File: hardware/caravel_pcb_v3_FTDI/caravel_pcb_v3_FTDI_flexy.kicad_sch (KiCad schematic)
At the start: 60 parts, among them J1 USB_B_Micro - 10118193-0001LF, J10 Conn_01x27_Female, J11 Conn_01x20_Female, J2 Conn_01x02_Female, J3 Conn_01x02_Female, J5 Conn_01x02_Male, J6 Conn_01x02_Male, J7 Conn_01x06_Female, J8 Conn_01x02_Male, J9 Conn_01x02_Male, SW1 SW_Push - SKQGADE010, T1 Logo, T2 Logo, U1 FT232H, U2 SN74LVC1G125DCKR, U3 SN74LVC1G125DCKR, U4 AZ1117CH-1.8TRG1, U5 AZ1117-3.3, U6 caravel_breakout, U7 W25Q32FVSS, X1 DSC6001_10MHZ, Y1 CSTNE12M0GH5L000R0

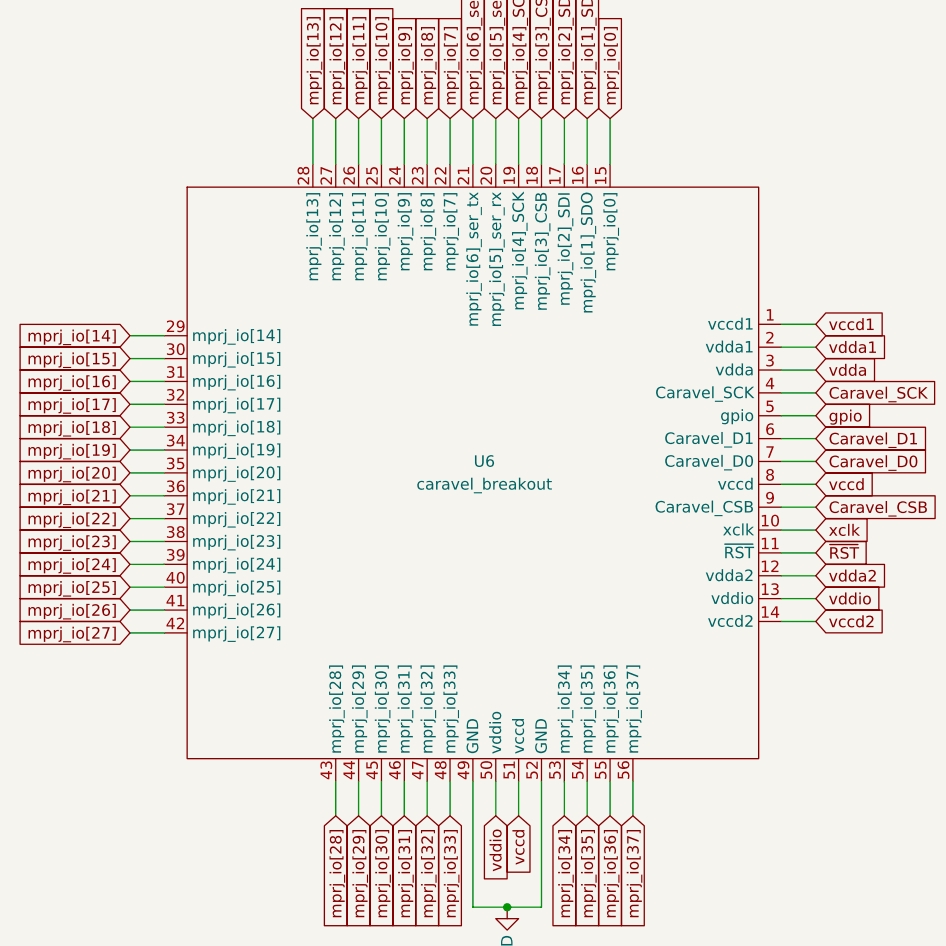
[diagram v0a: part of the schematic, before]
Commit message: fix caravel breakout pin mismatch
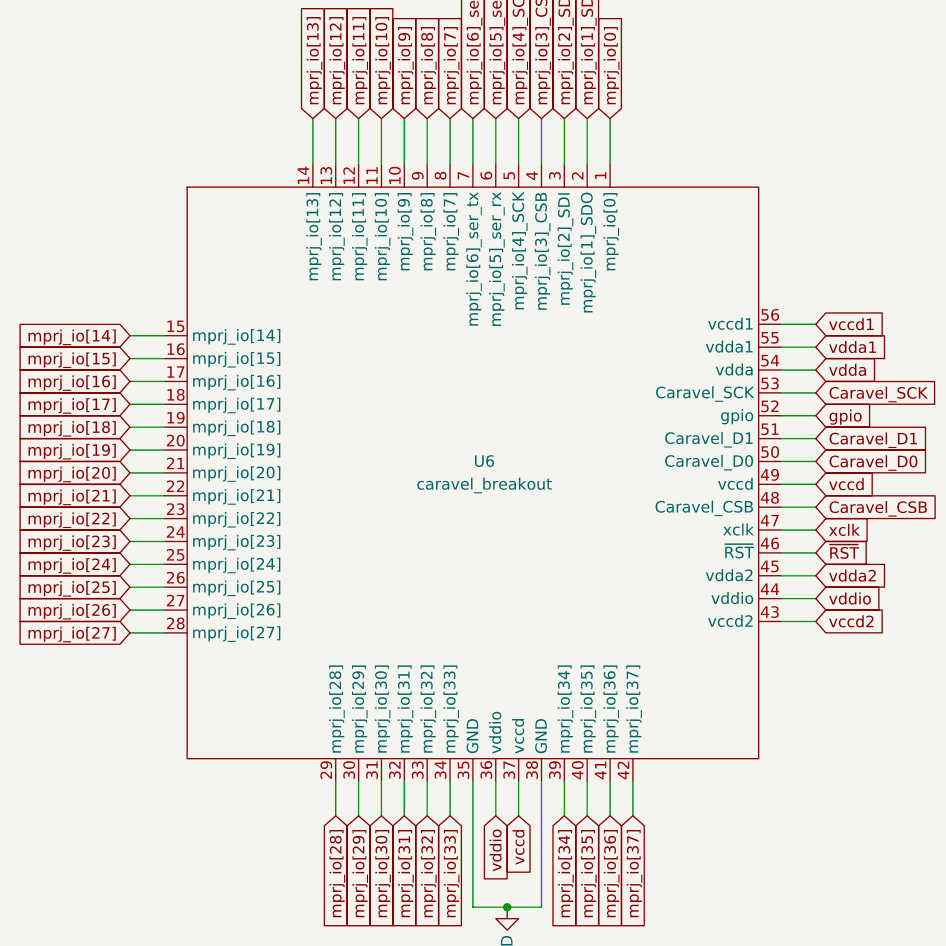
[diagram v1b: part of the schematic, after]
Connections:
- net +1V8: now also U6.37 (vccd), U6.49 (vccd); no longer U6.51 (vccd), U6.8 (vccd)
- net +3V3: now also U6.36 (vddio), U6.44 (vddio), U6.54 (vdda); no longer U6.13 (vddio), U6.3 (vdda), U6.50 (vddio)
- net Caravel_CSB: now also U6.48 (Caravel_CSB); no longer U6.9 (Caravel_CSB)
- net Caravel_D0: now also U6.50 (Caravel_D0); no longer U6.7 (Caravel_D0)
- net Caravel_D1: now also U6.51 (Caravel_D1); no longer U6.6 (Caravel_D1)
- net Caravel_SCK: now also U6.53 (Caravel_SCK); no longer U6.4 (Caravel_SCK)
- net GND: now also U6.35 (GND), U6.38 (GND); no longer U6.49 (GND), U6.52 (GND)
- net USB_CS1: now also U6.4 (mprj_io[3]_CSB); no longer U6.18 (mprj_io[3]_CSB)
- net USB_SCK_TXD: now also U6.5 (mprj_io[4]_SCK); no longer U6.19 (mprj_io[4]_SCK)
- net USB_SI: now also U6.2 (mprj_io[1]_SDO); no longer U6.16 (mprj_io[1]_SDO)
- net USB_SO_RXD: now also U6.3 (mprj_io[2]_SDI); no longer U6.17 (mprj_io[2]_SDI)
- net gpio: now also U6.52 (gpio); no longer U6.5 (gpio)
- net mprj_io[0]: now also U6.1 (mprj_io[0]); no longer U6.15 (mprj_io[0])
- net mprj_io[10]: now also U6.11 (mprj_io[10]); no longer U6.25 (mprj_io[10])
- net mprj_io[11]: now also U6.12 (mprj_io[11]); no longer U6.26 (mprj_io[11])
- net mprj_io[12]: now also U6.13 (mprj_io[12]); no longer U6.27 (mprj_io[12])
- net mprj_io[13]: now also U6.14 (mprj_io[13]); no longer U6.28 (mprj_io[13])
- net mprj_io[14]: now also U6.15 (mprj_io[14]); no longer U6.29 (mprj_io[14])
- net mprj_io[15]: now also U6.16 (mprj_io[15]); no longer U6.30 (mprj_io[15])
- net mprj_io[16]: now also U6.17 (mprj_io[16]); no longer U6.31 (mprj_io[16])
- net mprj_io[17]: now also U6.18 (mprj_io[17]); no longer U6.32 (mprj_io[17])
- net mprj_io[18]: now also U6.19 (mprj_io[18]); no longer U6.33 (mprj_io[18])
- net mprj_io[19]: now also U6.20 (mprj_io[19]); no longer U6.34 (mprj_io[19])
- net mprj_io[20]: now also U6.21 (mprj_io[20]); no longer U6.35 (mprj_io[20])
- net mprj_io[21]: now also U6.22 (mprj_io[21]); no longer U6.36 (mprj_io[21])
- net mprj_io[22]: now also U6.23 (mprj_io[22]); no longer U6.37 (mprj_io[22])
- net mprj_io[23]: now also U6.24 (mprj_io[23]); no longer U6.38 (mprj_io[23])
- net mprj_io[24]: now also U6.25 (mprj_io[24]); no longer U6.39 (mprj_io[24])
- net mprj_io[25]: now also U6.26 (mprj_io[25]); no longer U6.40 (mprj_io[25])
- net mprj_io[26]: now also U6.27 (mprj_io[26]); no longer U6.41 (mprj_io[26])
- net mprj_io[27]: now also U6.28 (mprj_io[27]); no longer U6.42 (mprj_io[27])
- net mprj_io[28]: now also U6.29 (mprj_io[28]); no longer U6.43 (mprj_io[28])
- net mprj_io[29]: now also U6.30 (mprj_io[29]); no longer U6.44 (mprj_io[29])
- net mprj_io[30]: now also U6.31 (mprj_io[30]); no longer U6.45 (mprj_io[30])
- net mprj_io[31]: now also U6.32 (mprj_io[31]); no longer U6.46 (mprj_io[31])
- net mprj_io[32]: now also U6.33 (mprj_io[32]); no longer U6.47 (mprj_io[32])
- net mprj_io[33]: now also U6.34 (mprj_io[33]); no longer U6.48 (mprj_io[33])
- net mprj_io[34]: now also U6.39 (mprj_io[34]); no longer U6.53 (mprj_io[34])
- net mprj_io[35]: now also U6.40 (mprj_io[35]); no longer U6.54 (mprj_io[35])
- net mprj_io[36]: now also U6.41 (mprj_io[36]); no longer U6.55 (mprj_io[36])
- net mprj_io[37]: now also U6.42 (mprj_io[37]); no longer U6.56 (mprj_io[37])
- net mprj_io[5]_ser_rx: now also U6.6 (mprj_io[5]_ser_rx); no longer U6.20 (mprj_io[5]_ser_rx)
- net mprj_io[6]_ser_tx: now also U6.7 (mprj_io[6]_ser_tx); no longer U6.21 (mprj_io[6]_ser_tx)
- net mprj_io[7]: now also U6.8 (mprj_io[7]); no longer U6.22 (mprj_io[7])
- net mprj_io[8]: now also U6.9 (mprj_io[8]); no longer U6.23 (mprj_io[8])
- net mprj_io[9]: now also U6.10 (mprj_io[9]); no longer U6.24 (mprj_io[9])
- net vccd1: now also U6.56 (vccd1); no longer U6.1 (vccd1)
- net vccd2: now also U6.43 (vccd2); no longer U6.14 (vccd2)
- net vdda1: now also U6.55 (vdda1); no longer U6.2 (vdda1)
- net vdda2: now also U6.45 (vdda2); no longer U6.12 (vdda2)
- net xclk: now also U6.47 (xclk); no longer U6.10 (xclk)
- net ~{RST}: now also U6.46 (~{RST}); no longer U6.11 (~{RST})

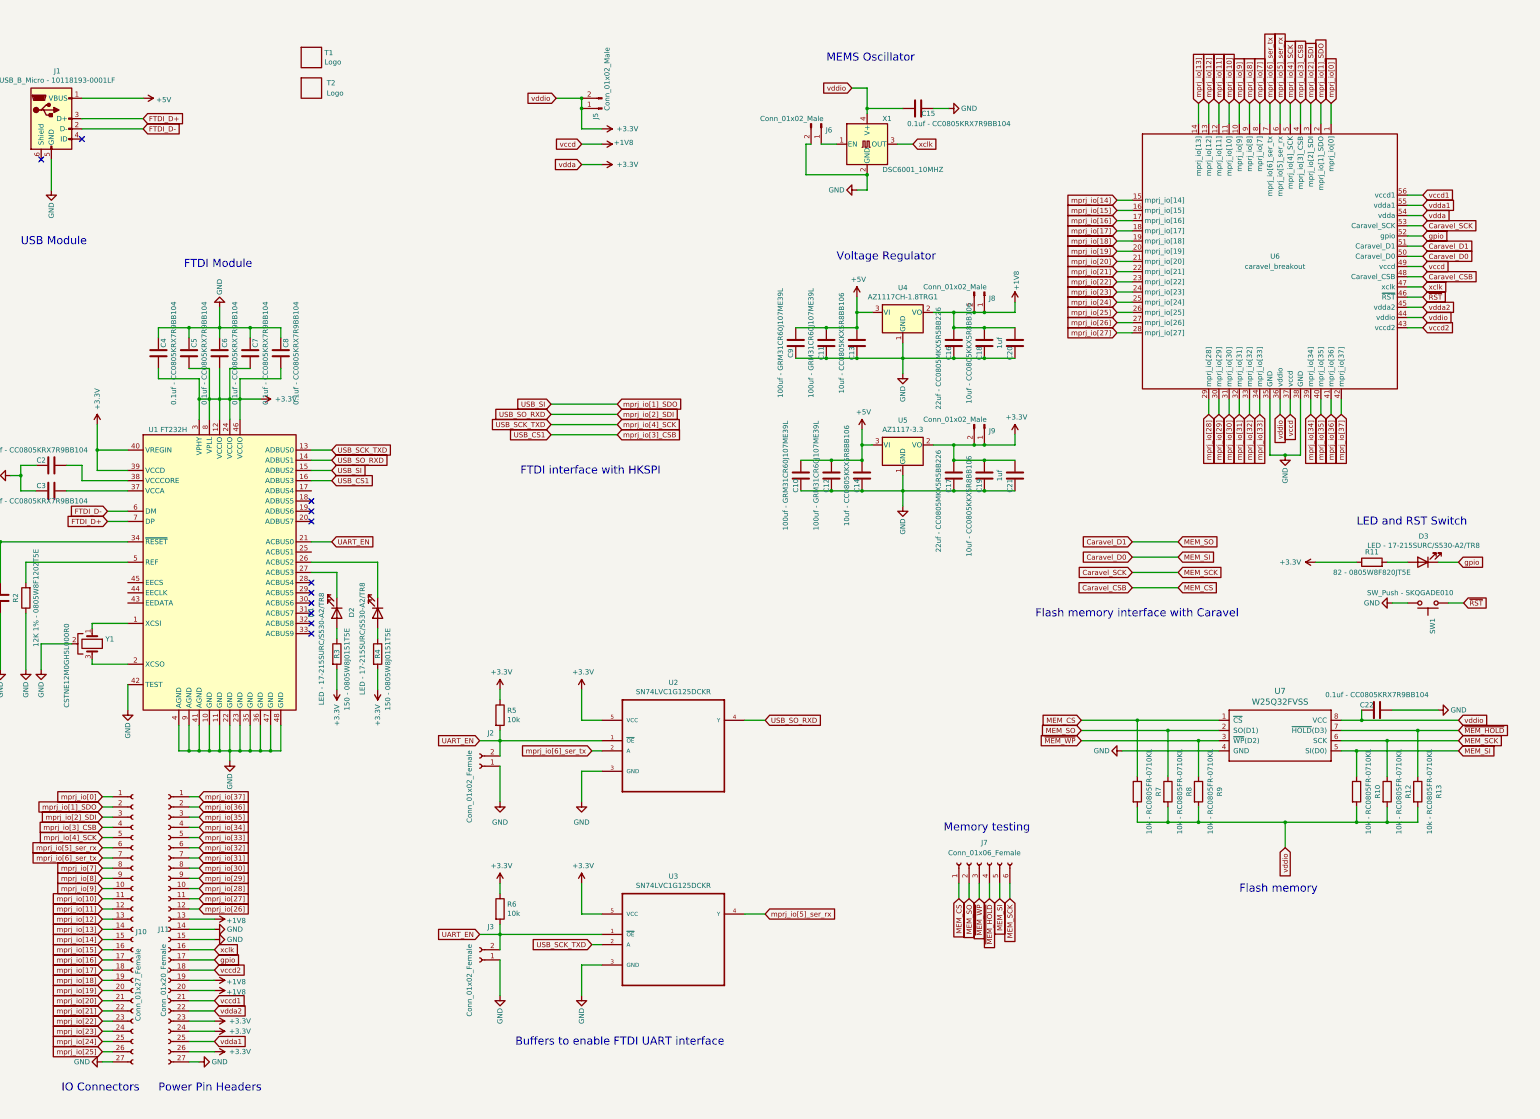
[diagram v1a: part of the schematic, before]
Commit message: update FTDI caravel board PCB and BOM (Rev 3C)
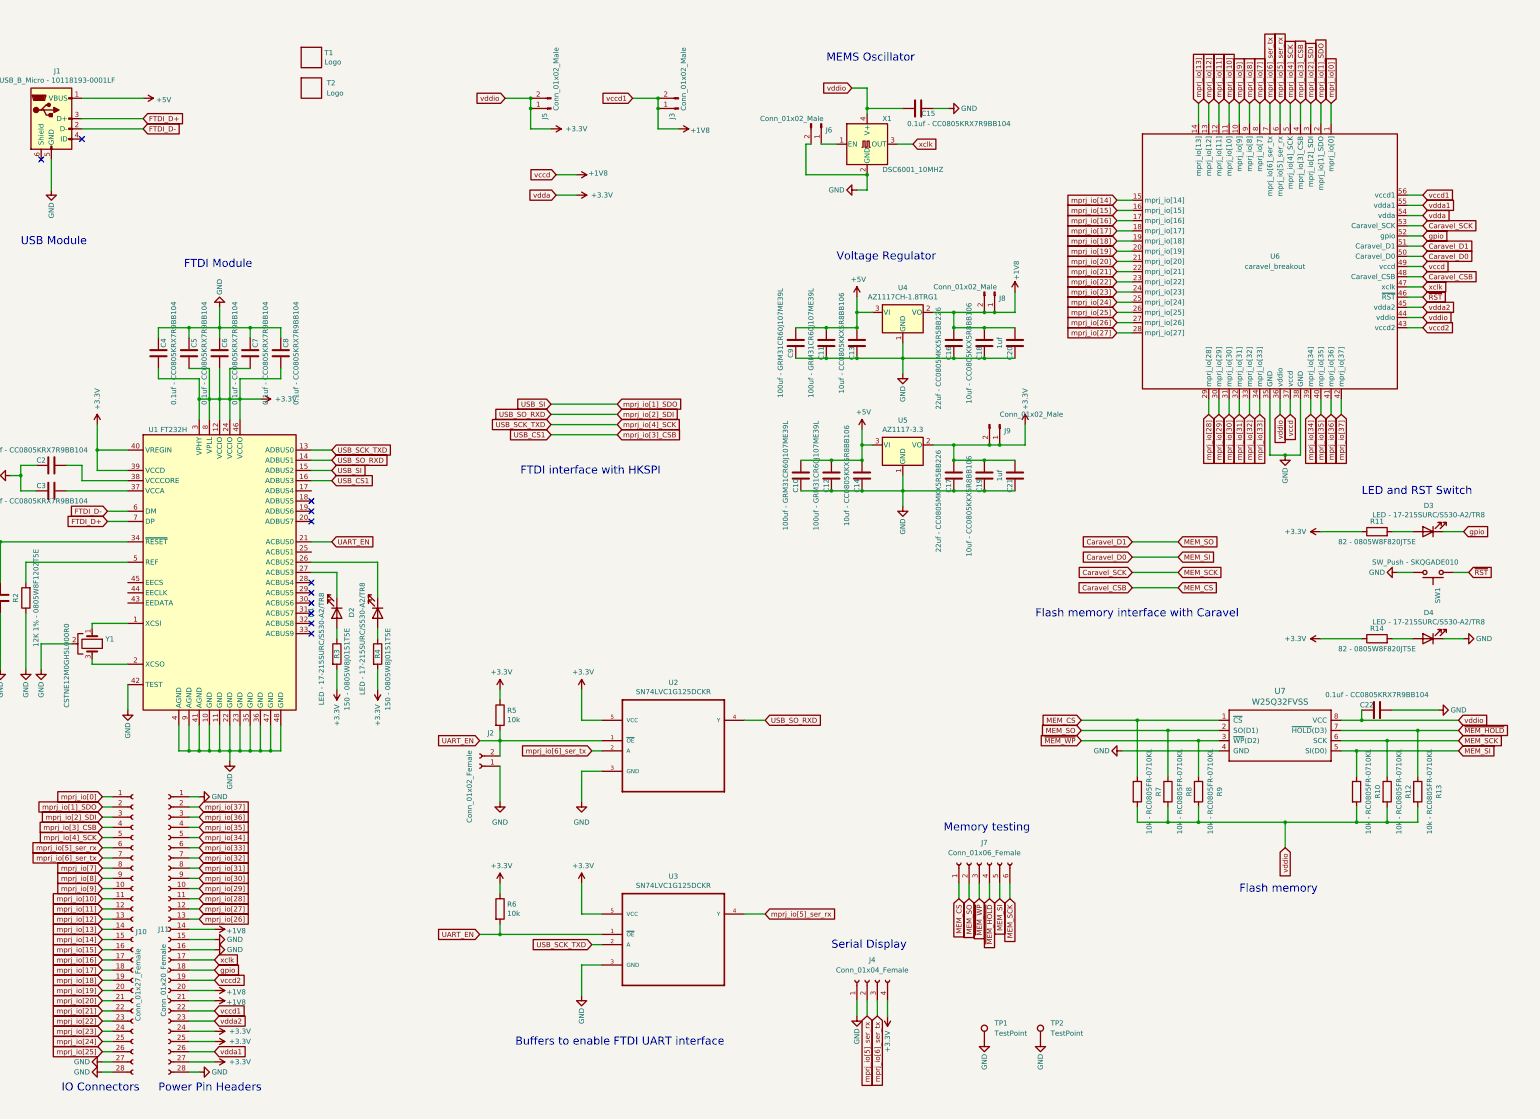
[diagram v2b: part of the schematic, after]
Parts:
- removed J3: Conn_01x02_Female, Connector_PinHeader_2.54mm:PinHeader_1x02_P2.54mm_Vertical, symbol Connector:Conn_01x02_Female
- added D4: LED - 17-215SURC/S530-A2/TR8, LED_SMD:LED_1206_3216Metric, symbol Device:LED
- added J3: Conn_01x02_Male, Connector_PinHeader_2.54mm:PinHeader_1x02_P2.54mm_Vertical, symbol Connector:Conn_01x02_Male
- added J4: Conn_01x04_Female, Connector_PinHeader_2.54mm:PinHeader_1x04_P2.54mm_Vertical, symbol Connector:Conn_01x04_Female
- added R14: 82 - 0805W8F820JT5E, Resistor_SMD:R_0805_2012Metric, symbol Device:R
- added TP1, TP2: TestPoint, TestPoint:TestPoint_Bridge_Pitch2.54mm_Drill1.0mm, symbol Connector:TestPoint
- J10, J11: symbol Connector:Conn_01x27_Female -> Connector:Conn_01x28_Female
- T1: symbol Caravel_pcb-rescue:Logo-Caravel_pcb -> Caravel_pcb_old:Logo-Caravel_pcb
- U2, U3: footprint strive_foot_prints:SOT65P210X110-5N -> SOT65P210X110-5N; symbol Caravel_pcb-rescue:SN74LVC1G125DCKR-SN74LVC1G125DCKR -> Caravel_pcb_old:SN74LVC1G125DCKR-SN74LVC1G125DCKR
- U7: symbol Caravel_pcb-rescue:W25Q32FVSS-Caravel_pcb -> Caravel_pcb_old:W25Q32FVSS-Caravel_pcb
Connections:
- net vccd1 is gone; now on net +1V8: J11.21 (Pin_21), U6.56 (vccd1)
- net +1V8: now also J11.14 (Pin_14), J11.22 (Pin_22), J3.1 (Pin_1), J3.2 (Pin_2); no longer J11.13 (Pin_13), J11.19 (Pin_19)
- net +3V3: now also J11.25 (Pin_25), J11.27 (Pin_27), J4.4 (Pin_4), R14.1; no longer J11.23 (Pin_23), J11.26 (Pin_26)
- net GND: now also J10.28 (Pin_28), J11.1 (Pin_1), J11.16 (Pin_16), J11.28 (Pin_28), D4.1 (K), J4.1 (Pin_1), TP1.1, TP2.1; no longer J11.14 (Pin_14), J11.27 (Pin_27)
- net gpio: now also J11.18 (Pin_18); no longer J11.17 (Pin_17)
- net mprj_io[26]: now also J11.13 (Pin_13); no longer J11.12 (Pin_12)
- net mprj_io[27]: now also J11.12 (Pin_12); no longer J11.11 (Pin_11)
- net mprj_io[28]: now also J11.11 (Pin_11); no longer J11.10 (Pin_10)
- net mprj_io[29]: now also J11.10 (Pin_10); no longer J11.9 (Pin_9)
- net mprj_io[30]: now also J11.9 (Pin_9); no longer J11.8 (Pin_8)
- net mprj_io[31]: now also J11.8 (Pin_8); no longer J11.7 (Pin_7)
- net mprj_io[32]: now also J11.7 (Pin_7); no longer J11.6 (Pin_6)
- net mprj_io[33]: now also J11.6 (Pin_6); no longer J11.5 (Pin_5)
- net mprj_io[34]: now also J11.5 (Pin_5); no longer J11.4 (Pin_4)
- net mprj_io[35]: now also J11.4 (Pin_4); no longer J11.3 (Pin_3)
- net mprj_io[36]: now also J11.3 (Pin_3); no longer J11.2 (Pin_2)
- net mprj_io[37]: now also J11.2 (Pin_2); no longer J11.1 (Pin_1)
- net mprj_io[5]_ser_rx: now also J4.2 (Pin_2)
- net mprj_io[6]_ser_tx: now also J4.3 (Pin_3)
- net vccd2: now also J11.19 (Pin_19); no longer J11.18 (Pin_18)
- net vdda1: now also J11.26 (Pin_26); no longer J11.25 (Pin_25)
- net vdda2: now also J11.23 (Pin_23); no longer J11.22 (Pin_22)
- net xclk: now also J11.17 (Pin_17); no longer J11.16 (Pin_16)
- new net: D4.2 (A), R14.2
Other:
- note added: "Serial Display"
- moved on the sheet: D3, J5, J8, J9, R11, SW1

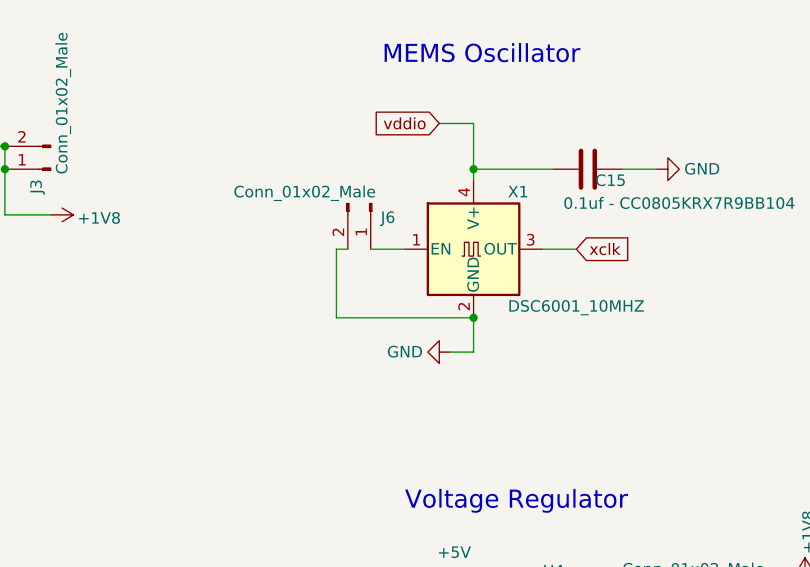
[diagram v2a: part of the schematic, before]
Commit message: update FTDI caravel board PCB (Rev 3D)
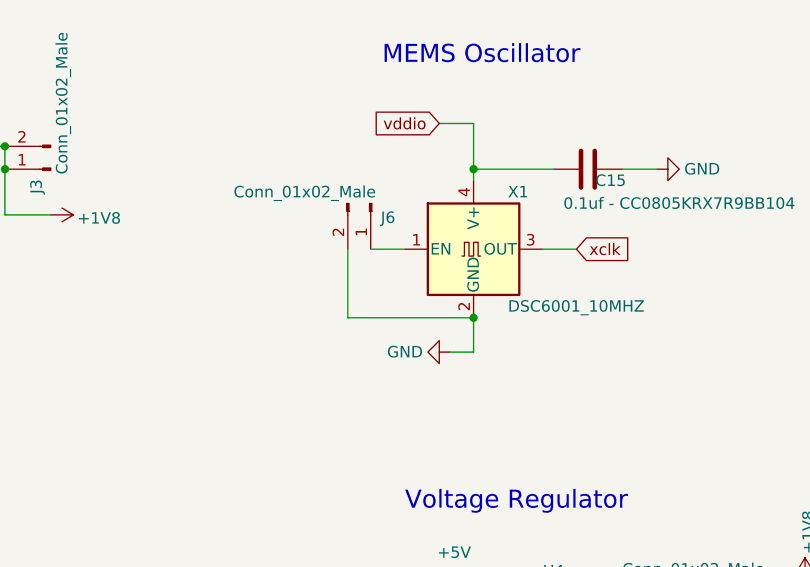
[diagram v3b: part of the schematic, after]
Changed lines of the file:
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@@
-    (stroke (width 0) (type default) (color 0 0 0 0))
-  )
-  (wire (pts (xy 231.14 44.45) (xy 232.41 44.45))
     (stroke (width 0) (type default) (color 0 0 0 0))
   )
@@
     (stroke (width 0) (type default) (color 0 0 0 0))
   )
-  (wire (pts (xy 231.14 44.45) (xy 231.14 52.07))
+  (wire (pts (xy 232.41 44.45) (xy 232.41 52.07))
     (stroke (width 0) (type default) (color 0 0 0 0))
   )
@@
     (stroke (width 0) (type default) (color 0 0 0 0))
   )
-  (wire (pts (xy 231.14 52.07) (xy 246.38 52.07))
-    (stroke (width 0) (type default) (color 0 0 0 0))
-  )
+  (wire (pts (xy 232.41 52.07) (xy 246.38 52.07))
+    (stroke (width 0) (type default) (color 0 0 0 0))
+  )
